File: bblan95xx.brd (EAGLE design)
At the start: 50 x 50 mm, 52 parts, among them IC1 LAN9512, IC2 93ST, Q1 25MHz

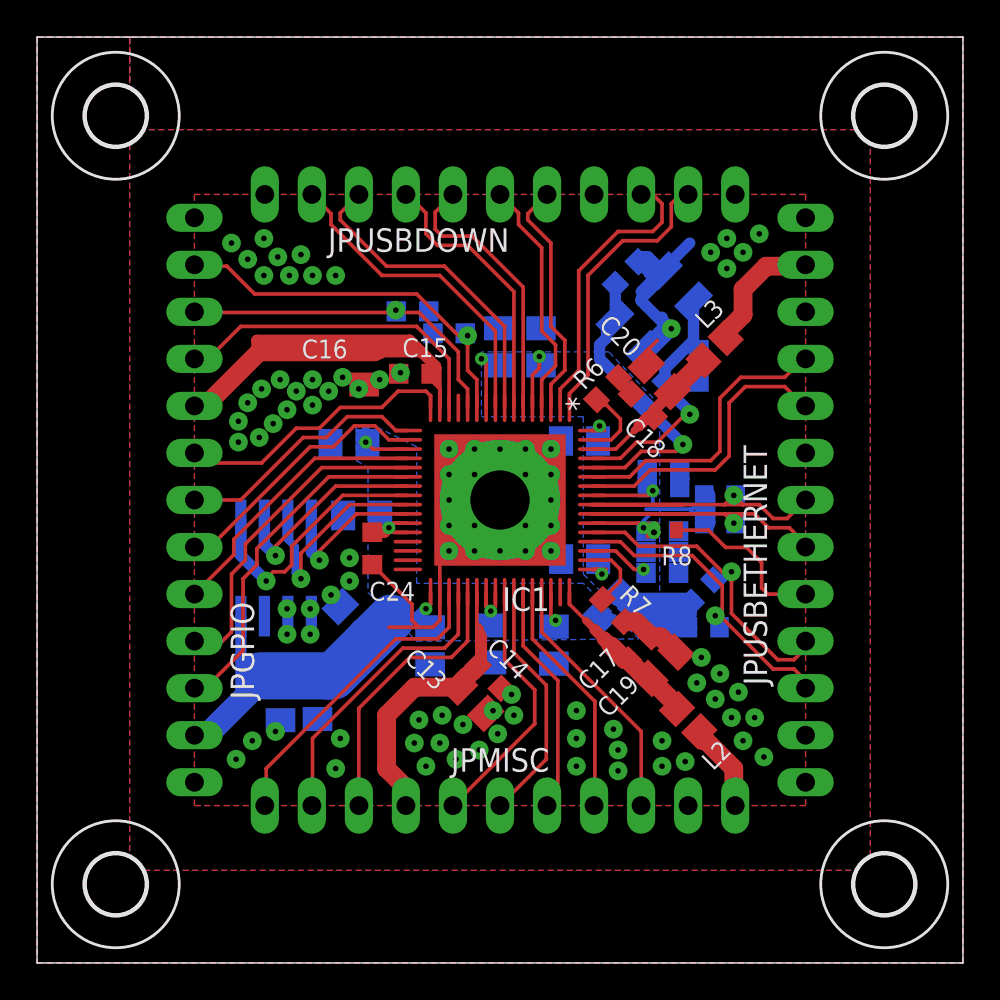
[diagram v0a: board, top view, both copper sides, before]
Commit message: improve pcb yield by optimizing PCB to revision 2
However the pinheaders remain either for castellations but more
because they are in the original schematic. (While the big
vias as holes instead are not)

When creating a panel the pinheaders can be removed.
But beware of the lables not to go away, too...

Signed-off-by: Stephan Baerwolf <stephan@matrixstorm.com>
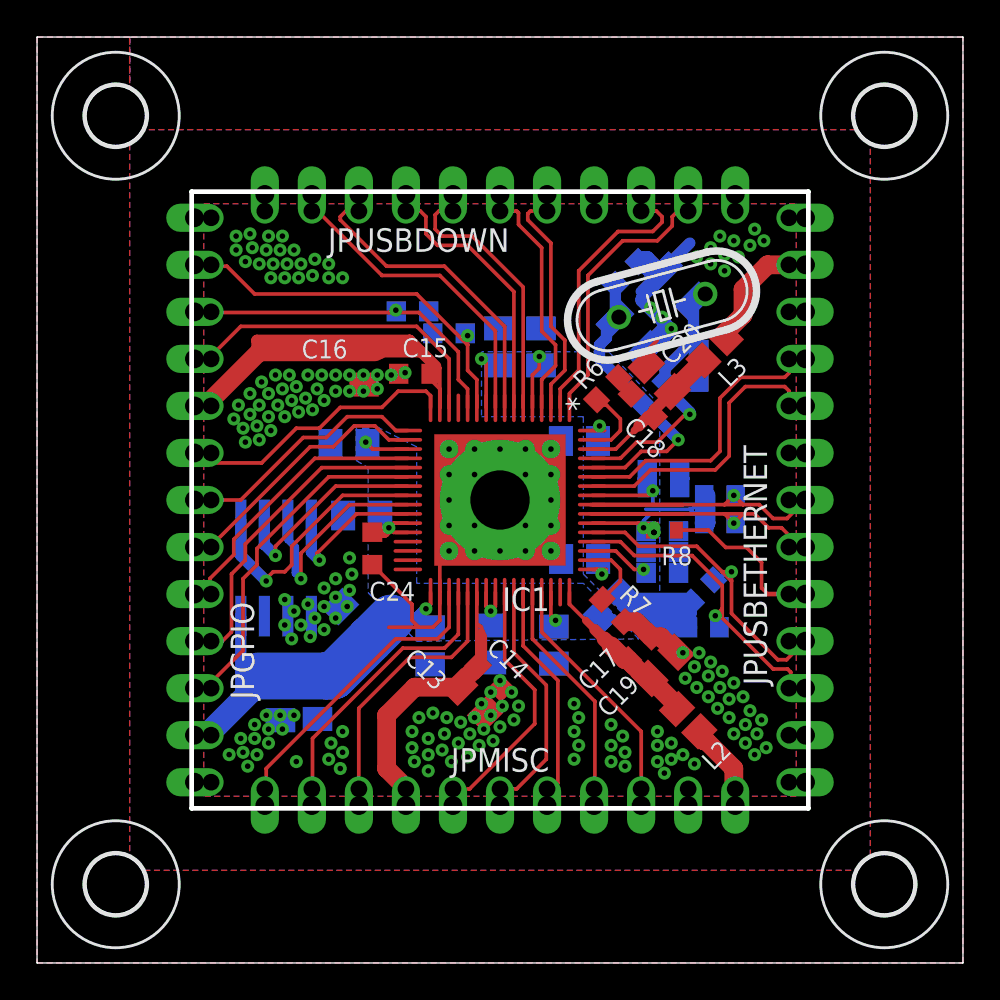
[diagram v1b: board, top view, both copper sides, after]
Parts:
- added Q2: (no value), crystal:HC49/S
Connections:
- net XI: now also Q2.2
- net XO: now also Q2.1
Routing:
- net VDD18CORE: track 97.3 -> 93.1 mm, vias 0 -> 2
- net VDD18EXTERNBRIDGE: track 47.4 -> 45.7 mm, vias 0 -> 2
- net PRTCTL3: track 15.3 -> 16.2 mm, vias 0 -> 1
- net XI: track 14.2 -> 15.0 mm
- net TXN: track 13.8 -> 14.5 mm, vias 1 -> 2
- net VBUS_DET: track 21.4 -> 22.0 mm, vias 1 -> 2
- net GPIO0: track 15.0 -> 15.6 mm, vias 0 -> 1
- net GPIO2: track 19.0 -> 19.6 mm, vias 0 -> 1
- net RXN: track 18.4 -> 18.9 mm, vias 1 -> 2
- net GPIO6: track 13.3 -> 13.8 mm, vias 0 -> 1
- net AUTOMDIX_EN: track 14.0 -> 14.6 mm, vias 0 -> 1
- net USBDP3: track 13.1 -> 13.6 mm, vias 0 -> 1
- net USBDM3: track 13.1 -> 13.6 mm, vias 0 -> 1
- net N$7: track 0.50 -> 0.00 mm
- net GPIO1: track 17.8 -> 18.2 mm, vias 0 -> 1
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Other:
- outline, holes or cut-outs redrawn
- board text added: "Aug. 2018"
- board text added: "C1"
- board text added: "C10"
- board text added: "C11"
- board text added: "C12"
- board text added: "C13"
- board text added: "C14"
- board text added: "C15"
- board text added: "C16"
- board text added: "C17"
- board text added: "C18"
- board text added: "C19"
- board text added: "C2"
- board text added: "C20"
- board text added: "C21"
- board text added: "C22"
- board text added: "C23"
- board text added: "C24"
- board text added: "C25"
- board text added: "C26"
- board text added: "C27"
- board text added: "C28"
- board text added: "C29"
- board text added: "C3"
- board text added: "C30"
- board text added: "C4"
- board text added: "C5"
- board text added: "C6"
- board text added: "C7"
- board text added: "C8"
- board text added: "C9"
- board text added: "IC1"
- board text added: "IC2"
- board text added: "JPGPIO"
- board text added: "JPMISC"
- board text added: "JPUSBDOWN"
- board text added: "JPUSBETHERNET"
- board text added: "L1"
- board text added: "L2"
- board text added: "L3"
- board text added: "Q1"
- board text added: "Q2"
- board text added: "R1"
- board text added: "R2"
- board text added: "R3"
- board text added: "R4"
- board text added: "R5"
- board text added: "R6"
- board text added: "R7"
- board text added: "R8"
- board text added: "rev. 2"
- board text removed: "Oct. 2016"
- board text removed: "rev. 1"
